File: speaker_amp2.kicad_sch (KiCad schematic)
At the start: 67 parts, among them J1 Molex_430450227, J2 Molex_430450227, J3 Molex_430450227, J4 Molex_430450227, J5 Molex_1053101106, U1 TAS5822MDCPR, U2 TAS5822MDCPR

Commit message: finished schematic with speaker buttons
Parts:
- added R11, R12, R13, R14, R15: 4.7k, Resistor_SMD:R_0805_2012Metric_Pad1.20x1.40mm_HandSolder, symbol Device:R
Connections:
- net +3.3V: now also J5.1
- net GND: now also R11.2, R12.2, R13.2, R14.2, R15.2
- net at J3.1: now also C38.1, C40.1, L6.2
- net at J3.2: now also C38.2, C39.1, L7.1
- net Previous: now reaches J5.2
- net Previous: now also MCU1.11 (GPIO27), R11.1
- net Next: now reaches J5.3
- net Next: now also MCU1.10 (GPIO26), R12.1
- net Volume-: now reaches J5.4
- net Volume-: now also MCU1.7 (GPIO32), R13.1
- net Volume+: now reaches J5.5
- net Volume+: now also MCU1.8 (GPIO33), R14.1
- net Play/Pause: now reaches J5.6
- net Play/Pause: now also MCU1.9 (GPIO25), R15.1
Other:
- note added: "Buttons"
- moved on the sheet: J5

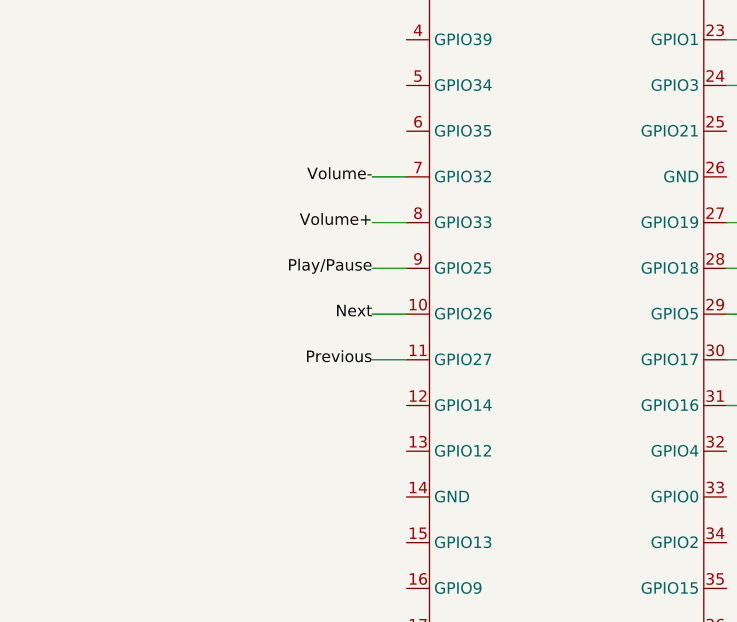
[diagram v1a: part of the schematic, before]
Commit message: added button connector to pcb
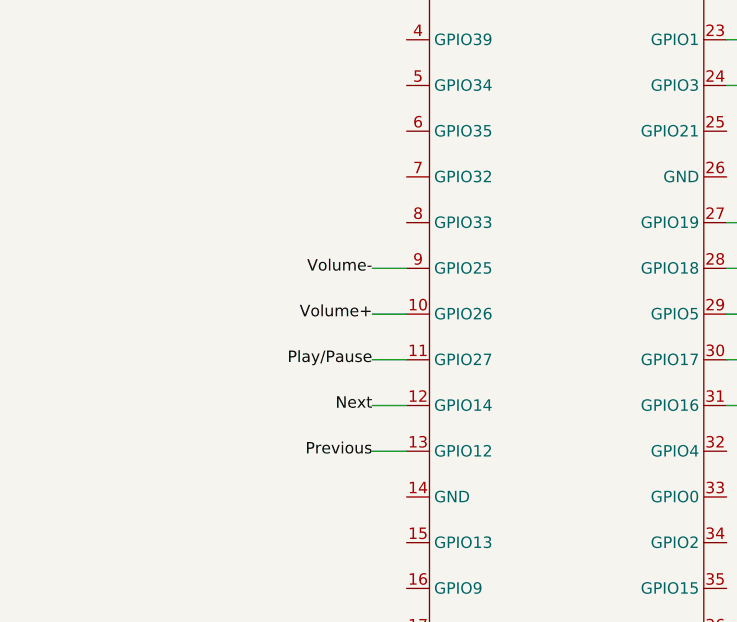
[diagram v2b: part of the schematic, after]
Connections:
- net Next: now also MCU1.12 (GPIO14); no longer MCU1.10 (GPIO26)
- net Play/Pause: now also MCU1.11 (GPIO27); no longer MCU1.9 (GPIO25)
- net Previous: now also MCU1.13 (GPIO12); no longer MCU1.11 (GPIO27)
- net Volume+: now also MCU1.10 (GPIO26); no longer MCU1.8 (GPIO33)
- net Volume-: now also MCU1.9 (GPIO25); no longer MCU1.7 (GPIO32)
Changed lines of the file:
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@@
 	(wire
 		(pts
-			(xy 62.23 151.13) (xy 66.04 151.13)
-		)
-		(stroke
-			(width 0)
-			(type default)
-		)
-	)
-	(wire
-		(pts
 			(xy 147.32 88.9) (xy 147.32 90.17)
 		)
@@
 	(wire
 		(pts
-			(xy 62.23 130.81) (xy 66.04 130.81)
-		)
-		(stroke
-			(width 0)
-			(type default)
-		)
-	)
-	(wire
-		(pts
 			(xy 269.24 176.53) (xy 273.05 176.53)
 		)
@@
 	(wire
 		(pts
-			(xy 62.23 146.05) (xy 66.04 146.05)
-		)
-		(stroke
-			(width 0)
-			(type default)
-		)
-	)
-	(wire
-		(pts
 			(xy 218.44 201.93) (xy 167.64 201.93)
 		)
@@
 	(wire
 		(pts
+			(xy 62.23 151.13) (xy 66.04 151.13)
+		)
+		(stroke
+			(width 0)
+			(type default)
+		)
+	)
+	(wire
+		(pts
 			(xy 218.44 194.31) (xy 177.8 194.31)
 		)
@@
 	(wire
 		(pts
-			(xy 62.23 135.89) (xy 66.04 135.89)
-		)
-		(stroke
-			(width 0)
-			(type default)
-		)
-	)
-	(wire
-		(pts
 			(xy 304.8 212.09) (xy 309.88 212.09)
 		)
@@
 	(wire
 		(pts
-			(xy 62.23 140.97) (xy 66.04 140.97)
-		)
-		(stroke
-			(width 0)
-			(type default)
-		)
-	)
-	(wire
-		(pts
 			(xy 64.77 60.96) (xy 64.77 63.5)
 		)
@@
 	(wire
 		(pts
+			(xy 62.23 161.29) (xy 66.04 161.29)
+		)
+		(stroke
+			(width 0)
+			(type default)
+		)
+	)
+	(wire
+		(pts
 			(xy 201.93 214.63) (xy 201.93 209.55)
 		)
@@
 	(wire
 		(pts
+			(xy 62.23 146.05) (xy 66.04 146.05)
+		)
+		(stroke
+			(width 0)
+			(type default)
+		)
+	)
+	(wire
+		(pts
 			(xy 218.44 119.38) (xy 205.74 119.38)
 		)
@@
 	(wire
 		(pts
+			(xy 62.23 140.97) (xy 66.04 140.97)
+		)
+		(stroke
+			(width 0)
+			(type default)
+		)
+	)
+	(wire
+		(pts
 			(xy 83.82 254) (xy 92.71 254)
 		)
@@
 	(wire
 		(pts
+			(xy 62.23 156.21) (xy 66.04 156.21)
+		)
+		(stroke
+			(width 0)
+			(type default)
+		)
+	)
+	(wire
+		(pts
 			(xy 229.87 264.16) (xy 242.57 264.16)
 		)
@@
 	)
 	(label "Volume-"
-		(at 62.23 130.81 180)
+		(at 62.23 140.97 180)
 		(fields_autoplaced yes)
 		(effects
@@
 	)
 	(label "Volume+"
-		(at 62.23 135.89 180)
+		(at 62.23 146.05 180)
 		(fields_autoplaced yes)
 		(effects
@@
 	)
 	(label "Next"
-		(at 62.23 146.05 180)
+		(at 62.23 156.21 180)
 		(fields_autoplaced yes)
 		(effects
@@
 	)
 	(label "Previous"
-		(at 62.23 151.13 180)
+		(at 62.23 161.29 180)
 		(fields_autoplaced yes)
 		(effects
@@
 	)
 	(label "Play{slash}Pause"
-		(at 62.23 140.97 180)
+		(at 62.23 151.13 180)
 		(fields_autoplaced yes)
 		(effects

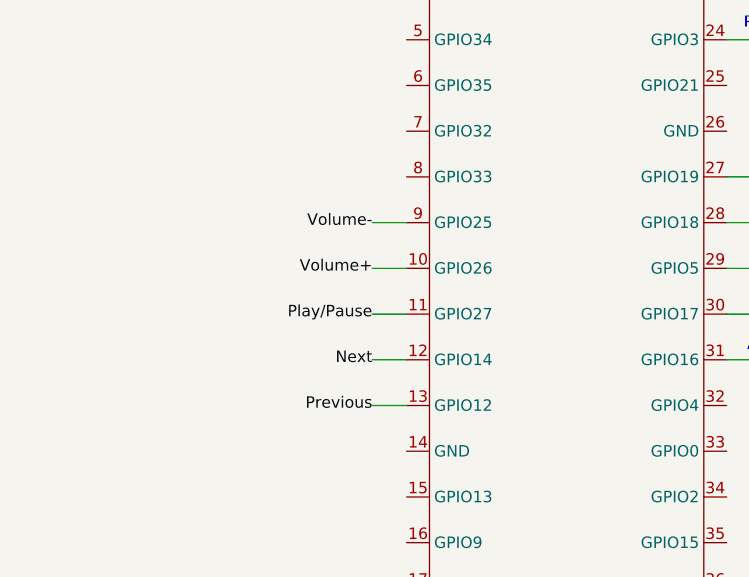
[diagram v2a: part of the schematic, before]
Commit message: placed 3.3V to pcb
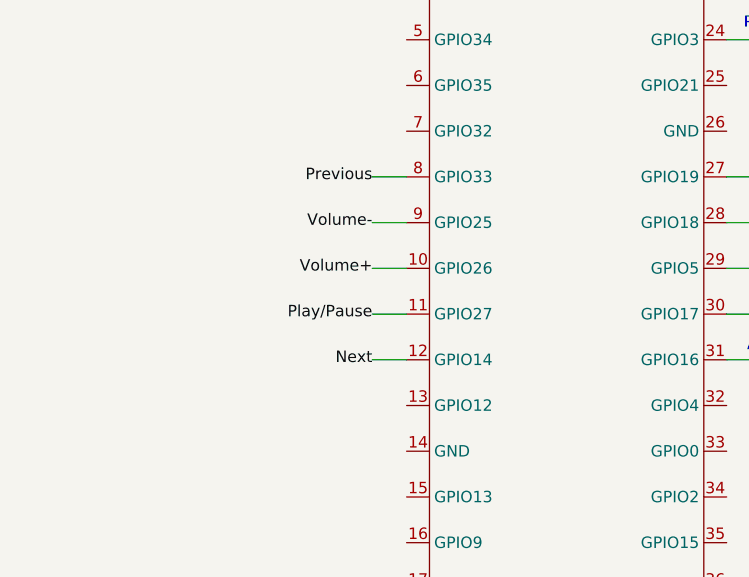
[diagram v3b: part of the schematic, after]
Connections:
- net Previous: now also MCU1.8 (GPIO33); no longer MCU1.13 (GPIO12)
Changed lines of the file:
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@@
 	(wire
 		(pts
+			(xy 62.23 135.89) (xy 66.04 135.89)
+		)
+		(stroke
+			(width 0)
+			(type default)
+		)
+	)
+	(wire
+		(pts
 			(xy 294.64 214.63) (xy 294.64 217.17)
 		)
@@
 	(wire
 		(pts
-			(xy 62.23 161.29) (xy 66.04 161.29)
-		)
-		(stroke
-			(width 0)
-			(type default)
-		)
-	)
-	(wire
-		(pts
 			(xy 201.93 214.63) (xy 201.93 209.55)
 		)
@@
 	)
 	(label "Previous"
-		(at 62.23 161.29 180)
+		(at 62.23 135.89 180)
 		(fields_autoplaced yes)
 		(effects

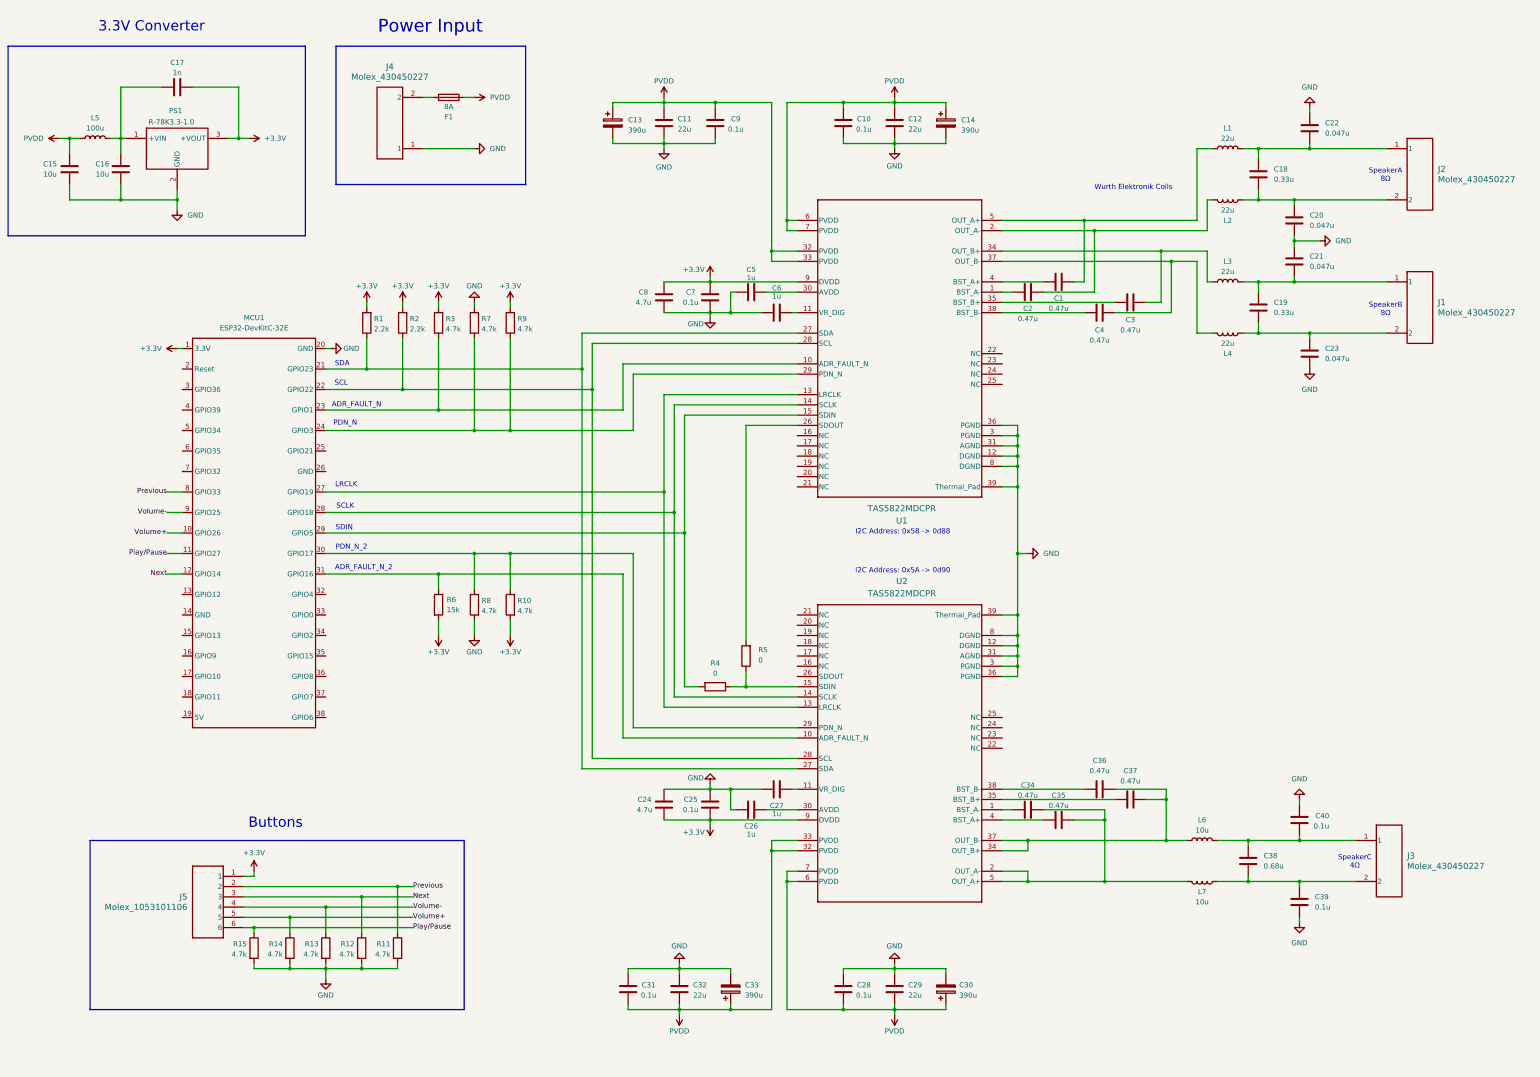
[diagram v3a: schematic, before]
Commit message: changed amplifiers in schematic to match PCB pins
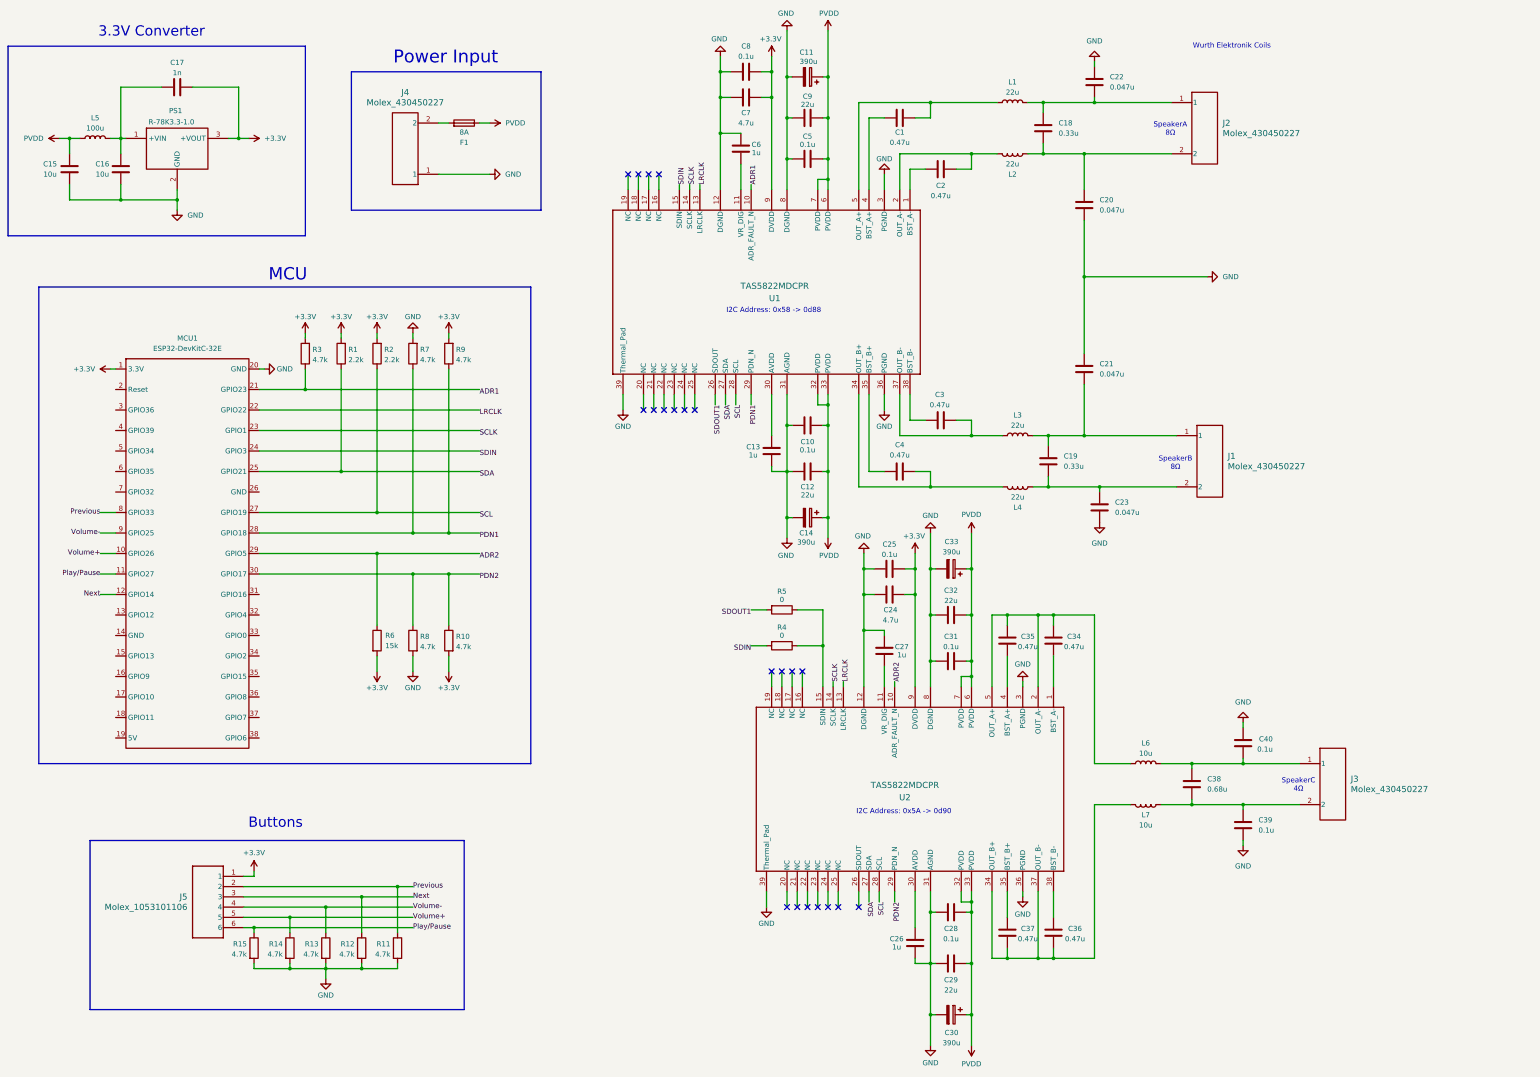
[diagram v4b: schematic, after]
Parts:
- removed C11: 22u, Capacitor_SMD:C_0805_2012Metric_Pad1.18x1.45mm_HandSolder, symbol Device:C
- removed C13: 390u, Capacitor_THT:CP_Radial_D8.0mm_P3.50mm, symbol Device:C_Polarized
- added C11: 390u, Capacitor_THT:CP_Radial_D8.0mm_P3.50mm, symbol Device:C_Polarized
- added C13: 1u, Capacitor_SMD:C_0603_1608Metric_Pad1.08x0.95mm_HandSolder, symbol Device:C
- C5: value 1u -> 0.1u; MouserLink https://gr.mouser.com/ProductDetail/TAIYO-YUDEN/MLAST168SB7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 -> https://gr.mouser.com/ProductDetail/KEMET/C0603C104J5RACTM?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
- C7: value 0.1u -> 4.7u; footprint Capacitor_SMD:C_0603_1608Metric_Pad1.08x0.95mm_HandSolder -> Capacitor_SMD:C_0805_2012Metric_Pad1.18x1.45mm_HandSolder; MouserLink https://gr.mouser.com/ProductDetail/KEMET/C0603C104J5RACTM?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 -> https://gr.mouser.com/ProductDetail/Murata-Electronics/GRM2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
- C8: value 4.7u -> 0.1u; footprint Capacitor_SMD:C_0805_2012Metric_Pad1.18x1.45mm_HandSolder -> Capacitor_SMD:C_0603_1608Metric_Pad1.08x0.95mm_HandSolder; MouserLink https://gr.mouser.com/ProductDetail/Murata-Electronics/GRM2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 -> https://gr.mouser.com/ProductDetail/KEMET/C0603C104J5RACTM?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
- C9: value 0.1u -> 22u; footprint Capacitor_SMD:C_0603_1608Metric_Pad1.08x0.95mm_HandSolder -> Capacitor_SMD:C_0805_2012Metric_Pad1.18x1.45mm_HandSolder; MouserLink https://gr.mouser.com/ProductDetail/KEMET/C0603C104J5RACTM?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 -> https://gr.mouser.com/ProductDetail/TDK/C2012X5R1V226M125AC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
- U1, U2: footprint DCP0038A-IPC_A -> Speaker Amp Lib:DCP0038A-IPC_A
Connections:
- net +3.3V: now also C7.1, C8.1; no longer C7.2, C8.2
- net GND: now also C26.1, C27.1, C6.2, C7.2, C8.2, C11.2, C13.1; no longer C26.2, C27.2, C6.1, C7.1, C8.1
- net PVDD: now also C5.2, C11.1
- net at U2.11 (VR_DIG): now also C27.2; no longer C27.1
- net ADR1: now reaches R3.1, U1.10 (ADR_FAULT_N)
- net ADR1: now also MCU1.21 (GPIO23); no longer MCU1.23 (GPIO1)
- net at U1.11 (VR_DIG): now also C6.1; no longer C6.2
- net at C35.1: now also C34.1, L6.1, U2.2 (OUT_A-), U2.5 (OUT_A+); no longer U2.4 (BST_A+)
- net at C4.2, L4.2: now also U1.34 (OUT_B+); no longer U1.37 (OUT_B-)
- net SDOUT1: now reaches R5.2, U1.26 (SDOUT)
- net at U1.30 (AVDD): now also C13.2; no longer C5.2
- net at C36.2, C37.2, U2.34 (OUT_B+)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: now also L7.2; no longer L6.1
- net SCL: now reaches R2.1, U1.28 (SCL), U2.28 (SCL)
- net SCL: now also MCU1.27 (GPIO19); no longer MCU1.22 (GPIO22)
- net ADR2: now reaches R6.1, U2.10 (ADR_FAULT_N)
- net ADR2: now also MCU1.29 (GPIO5); no longer MCU1.31 (GPIO16)
- net PDN1: now reaches R7.1, R9.1, U1.29 (PDN_N)
- net PDN1: now also MCU1.28 (GPIO18); no longer MCU1.24 (GPIO3)
- net SDA: now reaches R1.1, U1.27 (SDA), U2.27 (SDA)
- net SDA: now also MCU1.25 (GPIO21); no longer MCU1.21 (GPIO23)
- net LRCLK: now reaches U1.13 (LRCLK), U2.13 (LRCLK)
- net LRCLK: now also MCU1.22 (GPIO22); no longer MCU1.27 (GPIO19)
- net SCLK: now reaches U1.14 (SCLK), U2.14 (SCLK)
- net SCLK: now also MCU1.23 (GPIO1); no longer MCU1.28 (GPIO18)
- net SDIN: now reaches R4.2, U1.15 (SDIN)
- net SDIN: now also MCU1.24 (GPIO3); no longer MCU1.29 (GPIO5)
- net at C3.2, L3.1: now also U1.37 (OUT_B-); no longer U1.34 (OUT_B+)
- net at U1.35 (BST_B+): now also C4.1; no longer C3.1
- net at U1.38 (BST_B-): now also C3.1; no longer C4.1
- net PDN2: now reaches MCU1.30 (GPIO17), R10.1, R8.1, U2.29 (PDN_N)
- net at U2.30 (AVDD): now also C26.2; no longer C26.1
- net at U2.1 (BST_A-): now also C34.2; no longer C34.1
- new net: C35.2, U2.4 (BST_A+)
- no-connect marks 0 -> 21
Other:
- note added: "MCU"
- note removed: "ADR_FAULT_N"
- note removed: "ADR_FAULT_N_2"
- note removed: "LRCLK"
- note removed: "PDN_N"
- note removed: "PDN_N_2"
- note removed: "SCL"
- note removed: "SCLK"
- note removed: "SDA"
- note removed: "SDIN"
- moved on the sheet: C1, C10, C12, C14, C18, C19, C2, C20, C21, C22, C23, C26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

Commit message: placed amp ics, did low-voltage connections
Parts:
- U1, U2: footprint Speaker Amp Lib:DCP0038A-IPC_A -> Speaker Amp Lib:DCP0038A-IPC_B
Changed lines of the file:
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@@
 			)
 		)
-		(property "Footprint" "Speaker Amp Lib:DCP0038A-IPC_A"
+		(property "Footprint" "Speaker Amp Lib:DCP0038A-IPC_B"
 			(at 243.84 60.96 0)
 			(effects
@@
 			)
 		)
-		(property "Footprint" "Speaker Amp Lib:DCP0038A-IPC_A"
-			(at 279.4 184.15 0)
+		(property "Footprint" "Speaker Amp Lib:DCP0038A-IPC_B"
+			(at 278.13 184.15 0)
 			(effects
 				(font
@@
 		)
 		(property "Datasheet" "TAS5822MDCPR"
-			(at 279.4 184.15 0)
-			(effects
-				(font
+			(at 278.13 184.15 0)
+			(effects
+				(font
